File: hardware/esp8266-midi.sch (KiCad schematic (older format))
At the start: 26 parts, among them J1 MIDI in, J2 MIDI out, J3 TTL-232R-3V3 connector, J4 Bat+, J5 Bat-, J6 MIDI through, J7 Debug serial out, U1 ESP-12E, U2 6N138, U3 LD1117S50TR_SOT223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

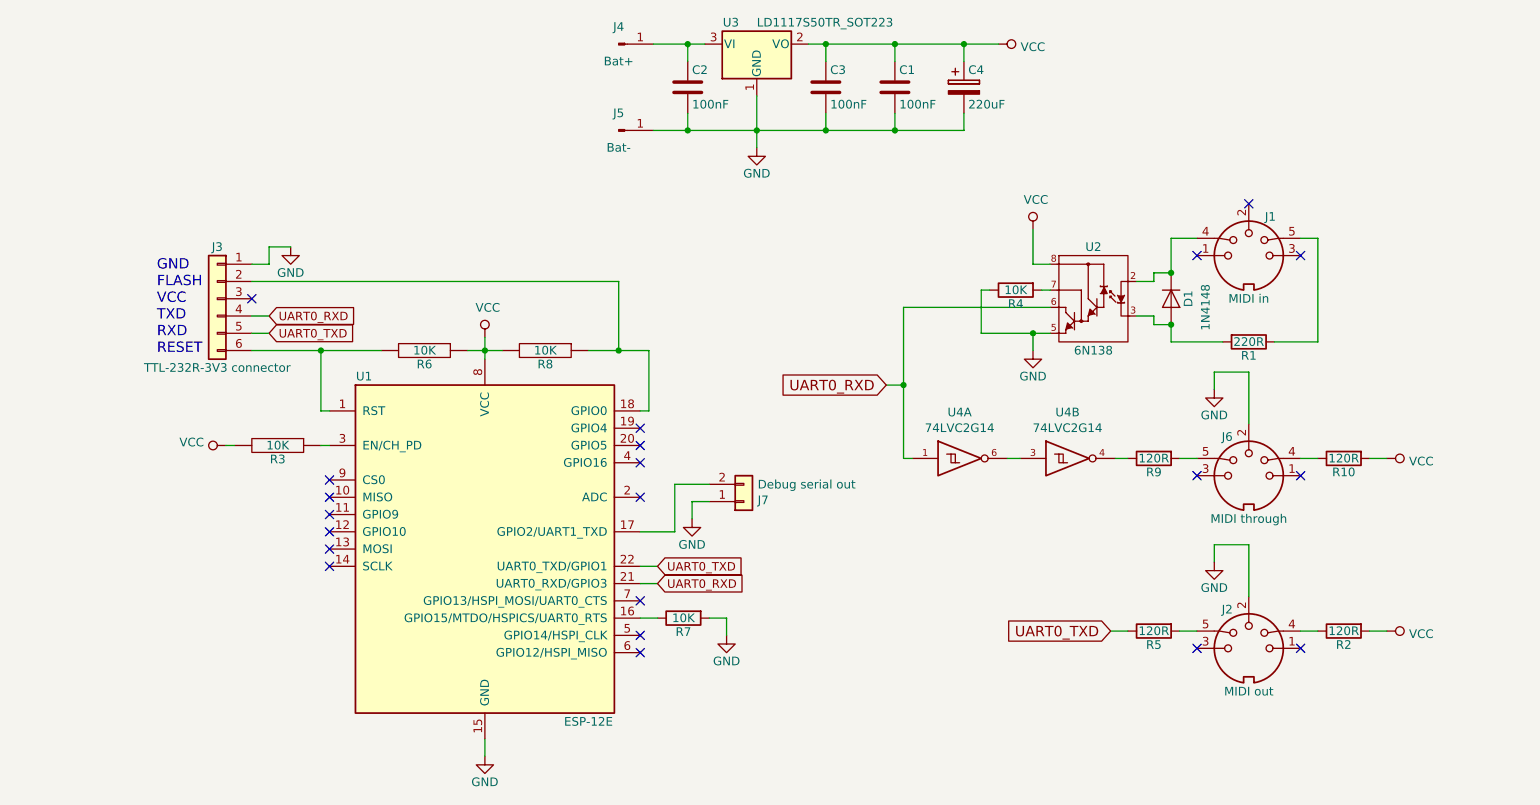
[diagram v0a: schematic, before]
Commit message: Misc: add some extra labels to have little more meaningful net names
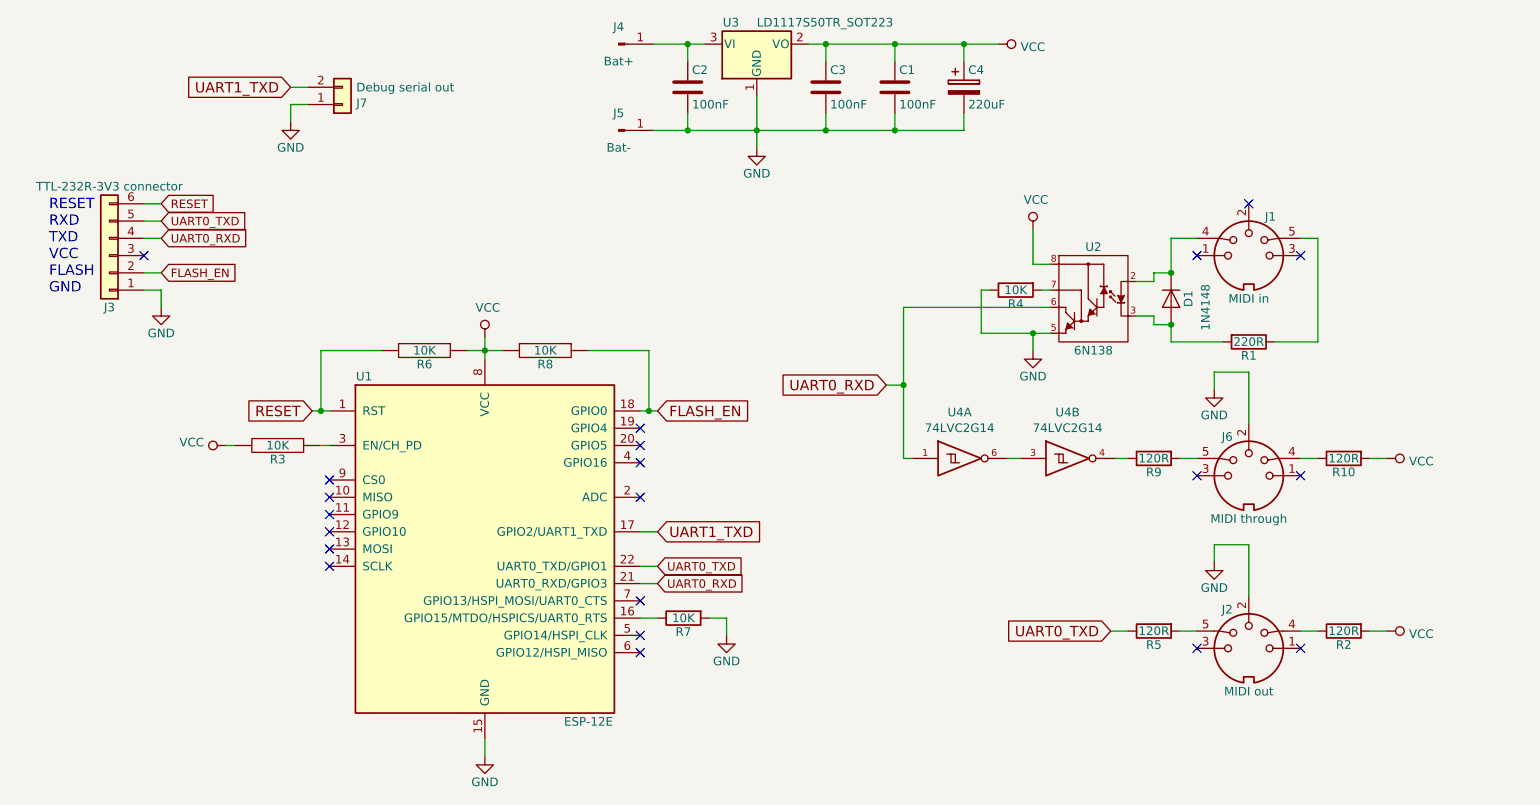
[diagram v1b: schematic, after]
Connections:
- net FLASH_EN: now reaches J3.2 (Pin_2), R8.1, U1.18 (GPIO0)
- net RESET: now reaches J3.6 (Pin_6), R6.2, U1.1 (RST)
- net UART1_TXD: now reaches J7.2 (Pin_2), U1.17 (GPIO2/UART1_TXD)
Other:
- note added: "RESET\nRXD\nTXD\nVCC\nFLASH\nGND\n"
- note removed: "GND\nFLASH\nVCC\nTXD\nRXD\nRESET"
- moved on the sheet: J3, J7
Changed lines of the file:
@@
 	-1   0    0    -1
 $EndComp
-Text Notes 2300 3475 0    60   ~ 0
-GND\nFLASH\nVCC\nTXD\nRXD\nRESET
+Text Notes 1675 3125 0    60   ~ 0
+RESET\nRXD\nTXD\nVCC\nFLASH\nGND\n
 NoConn ~ 8325 5175
 NoConn ~ 8925 5175
@@
 	4100 3450 4200 3450
 Wire Wire Line
-	4800 3450 4975 3450
-Wire Wire Line
 	5150 3450 5150 3800
 Wire Wire Line
@@
 L Connector1:Conn_01x06 J3
 U 1 1 5AA1FA8A
-P 2650 3150
-F 0 "J3" H 2650 3450 50  0000 C CNN
-F 1 "TTL-232R-3V3 connector" H 2650 2750 50  0000 C CNN
-F 2 "Pin_Headers:Pin_Header_Straight_1x06_Pitch2.54mm" H 2650 3150 50  0001 C CNN
-F 3 "" H 2650 3150 50  0001 C CNN
-	1    2650 3150
-	-1   0    0    -1
-$EndComp
-NoConn ~ 2850 3150
+P 2025 2900
+F 0 "J3" H 2025 3200 50  0000 C CNN
+F 1 "TTL-232R-3V3 connector" H 2025 2500 50  0000 C CNN
+F 2 "Pin_Headers:Pin_Header_Straight_1x06_Pitch2.54mm" H 2025 2900 50  0001 C CNN
+F 3 "" H 2025 2900 50  0001 C CNN
+	1    2025 2900
+	-1   0    0    1
+$EndComp
+NoConn ~ 2225 2900
 NoConn ~ 5100 4100
 Wire Wire Line
@@
 Wire Wire Line
 	6625 3200 7475 3200
-Text GLabel 2950 3350 2    49   Input ~ 0
+Text GLabel 2325 2700 2    49   Input ~ 0
 UART0_TXD
-Text GLabel 2950 3250 2    49   Input ~ 0
+Text GLabel 2325 2800 2    49   Input ~ 0
 UART0_RXD
 Wire Wire Line
@@
 Wire Wire Line
 	3250 3450 3600 3450
-Wire Wire Line
-	2850 3450 3250 3450
-Connection ~ 3250 3450
-Wire Wire Line
-	4975 3050 4975 3450
-Connection ~ 4975 3450
-Wire Wire Line
-	4975 3450 5150 3450
-Wire Wire Line
-	2850 3050 4975 3050
 $Comp
 L power1:GND #PWR05
 U 1 1 5C00E9E6
-P 3075 2850
-F 0 "#PWR05" H 3075 2600 50  0001 C CNN
-F 1 "GND" H 3075 2700 50  0000 C CNN
-F 2 "" H 3075 2850 50  0001 C CNN
-F 3 "" H 3075 2850 50  0001 C CNN
-	1    3075 2850
+P 2325 3200
+F 0 "#PWR05" H 2325 2950 50  0001 C CNN
+F 1 "GND" H 2325 3050 50  0000 C CNN
+F 2 "" H 2325 3200 50  0001 C CNN
+F 3 "" H 2325 3200 50  0001 C CNN
+	1    2325 3200
 	-1   0    0    -1
 $EndComp
-Wire Wire Line
-	2850 2950 2950 2950
-Wire Wire Line
-	2950 2950 2950 2850
-Wire Wire Line
-	2950 2850 3075 2850
-Wire Wire Line
-	2850 3250 2950 3250
-Wire Wire Line
-	2850 3350 2950 3350
 Text GLabel 5200 4700 2    49   Input ~ 0
 UART0_TXD
@@
 L Connector1:Conn_01x02 J7
 U 1 1 5C040B63
-P 5700 4325
-F 0 "J7" H 5780 4317 50  0000 L CNN
-F 1 "Debug serial out" H 5780 4226 50  0000 L CNN
-F 2 "Pin_Headers:Pin_Header_Straight_1x02_Pitch2.54mm" H 5700 4325 50  0001 C CNN
-F 3 "~" H 5700 4325 50  0001 C CNN
-	1    5700 4325
+P 3375 2025
+F 0 "J7" H 3455 2017 50  0000 L CNN
+F 1 "Debug serial out" H 3455 1926 50  0000 L CNN
+F 2 "Pin_Headers:Pin_Header_Straight_1x02_Pitch2.54mm" H 3375 2025 50  0001 C CNN
+F 3 "~" H 3375 2025 50  0001 C CNN
+	1    3375 2025
 	1    0    0    1
 $EndComp
-Wire Wire Line
-	5300 4500 5300 4225
 $Comp
 L power1:GND #PWR014
 U 1 1 5C0439C0
-P 5400 4425
-F 0 "#PWR014" H 5400 4175 50  0001 C CNN
-F 1 "GND" H 5400 4275 50  0000 C CNN
-F 2 "" H 5400 4425 50  0001 C CNN
-F 3 "" H 5400 4425 50  0001 C CNN
-	1    5400 4425
+P 3075 2125
+F 0 "#PWR014" H 3075 1875 50  0001 C CNN
+F 1 "GND" H 3075 1975 50  0000 C CNN
+F 2 "" H 3075 2125 50  0001 C CNN
+F 3 "" H 3075 2125 50  0001 C CNN
+	1    3075 2125
 	-1   0    0    -1
 $EndComp
 Wire Wire Line
-	5400 4425 5400 4325
-Wire Wire Line
-	5100 4500 5300 4500
+	3075 2125 3075 2025
 $Comp
 L esp8266-midi-rescue:C-RESCUE-esp8266-midi C1
@@
 	6975 1675 7175 1675
 $Comp
-L power:VCC #PWR?
+L power:VCC #PWR0101
 U 1 1 5C039076
 P 7175 1675
-F 0 "#PWR?" H 7175 1525 50  0001 C CNN
+F 0 "#PWR0101" H 7175 1525 50  0001 C CNN
 F 1 "VCC" V 7192 1803 50  0000 L CNN
 F 2 "" H 7175 1675 50  0001 C CNN
@@
 $EndComp
 $Comp
-L power:VCC #PWR?
+L power:VCC #PWR0102
 U 1 1 5C03C08A
 P 4200 3375
-F 0 "#PWR?" H 4200 3225 50  0001 C CNN
+F 0 "#PWR0102" H 4200 3225 50  0001 C CNN
 F 1 "VCC" H 4217 3548 50  0000 C CNN
 F 2 "" H 4200 3375 50  0001 C CNN
@@
 $EndComp
 $Comp
-L power:VCC #PWR?
+L power:VCC #PWR0103
 U 1 1 5C04A4B7
 P 2700 4000
-F 0 "#PWR?" H 2700 3850 50  0001 C CNN
+F 0 "#PWR0103" H 2700 3850 50  0001 C CNN
 F 1 "VCC" V 2718 4127 50  0000 L CNN
 F 2 "" H 2700 4000 50  0001 C CNN
@@
 $EndComp
 $Comp
-L power:VCC #PWR?
+L power:VCC #PWR0104
 U 1 1 5C0530C7
 P 7375 2750
-F 0 "#PWR?" H 7375 2600 50  0001 C CNN
+F 0 "#PWR0104" H 7375 2600 50  0001 C CNN
 F 1 "VCC" H 7392 2923 50  0000 C CNN
 F 2 "" H 7375 2750 50  0001 C CNN
@@
 $EndComp
 $Comp
-L power:VCC #PWR?
+L power:VCC #PWR0105
 U 1 1 5C05BBAA
 P 9425 4075
-F 0 "#PWR?" H 9425 3925 50  0001 C CNN
+F 0 "#PWR0105" H 9425 3925 50  0001 C CNN
 F 1 "VCC" V 9442 4203 50  0000 L CNN
 F 2 "" H 9425 4075 50  0001 C CNN
@@
 $EndComp
 $Comp
-L power:VCC #PWR?
+L power:VCC #PWR0106
 U 1 1 5C06708F
 P 9425 5075
-F 0 "#PWR?" H 9425 4925 50  0001 C CNN
+F 0 "#PWR0106" H 9425 4925 50  0001 C CNN
 F 1 "VCC" V 9442 5203 50  0000 L CNN
 F 2 "" H 9425 5075 50  0001 C CNN
@@
 $EndComp
 Wire Wire Line
-	5400 4325 5500 4325
-Wire Wire Line
-	5300 4225 5500 4225
+	3075 2025 3175 2025
+Text GLabel 5200 4500 2    60   Input ~ 0
+UART1_TXD
+Wire Wire Line
+	5100 4500 5200 4500
+Text GLabel 3075 1925 0    60   Input ~ 0
+UART1_TXD
+Wire Wire Line
+	3075 1925 3175 1925
+Text GLabel 5200 3800 2    60   Input ~ 0
+FLASH_EN
+Wire Wire Line
+	5150 3800 5200 3800
+Connection ~ 5150 3800
+Wire Wire Line
+	4800 3450 5150 3450
+Text GLabel 2325 3000 2    49   Input ~ 0
+FLASH_EN
+Text GLabel 3200 3800 0    60   Input ~ 0
+RESET
+Wire Wire Line
+	3200 3800 3250 3800
+Connection ~ 3250 3800
+Text GLabel 2325 2600 2    49   Input ~ 0
+RESET
+Wire Wire Line
+	2225 3100 2325 3100
+Wire Wire Line
+	2325 3100 2325 3200
+Wire Wire Line
+	2225 3000 2325 3000
+Wire Wire Line
+	2225 2600 2325 2600
+Wire Wire Line
+	2225 2800 2325 2800
+Wire Wire Line
+	2225 2700 2325 2700
 $EndSCHEMATC

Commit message: Use alternative uart0 pins for midi i/o
uart0 pushes bunch of rubbish messages on boot up. This means some pretty random
messages on the midi out port. To fix this midi i/o uses alternative uart0 pins
which can be enabled after microcontroller is booted by calling 'Serial.swap()'.

Alternative TX pin needs to be pulled down during boot, but a connected midi
instrument pull it up. Therefore the buffering using the same dual nand
(74LVC2G14) as for the midi through port.
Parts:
- added C5: 100nF, Capacitors_SMD:C_0805_HandSoldering, symbol esp8266-midi-rescue:C-RESCUE-esp8266-midi
- added U5: 74LVC2G14, TO_SOT_Packages_SMD:SOT-23-6_Handsoldering, symbol 74xGxx:74LVC2G14
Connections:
- net GND: now also R7.1, C5.2, U5.2 (GND), U5.2 (GND); no longer R7.2
- net UART0_RXD: no longer U2.6 (Vo), U4.1
- net UART0_TXD: no longer R5.1
- net VCC: now also C5.1, U5.5 (VCC), U5.5 (VCC)
- net UART0_ALT_TXD: now reaches U1.16 (GPIO15/MTDO/HSPICS/UART0_RTS)
- net UART0_ALT_TXD: now also R7.2, U5.1; no longer R7.1
- net UART0_ALT_RXD: now reaches U1.7 (GPIO13/HSPI_MOSI/UART0_CTS)
- net UART0_ALT_RXD: now also U2.6 (Vo), U4.1
- new net: R5.1, U5.4
- new net: U5.3, U5.6
- no-connect marks 21 -> 20
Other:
- moved on the sheet: C4, D1, J1, J2, J6, R1, R10, R2, R4, R5, R7, R9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

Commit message: Kicad5 update woes again: eeschema rescues
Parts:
- C4: symbol device:CP -> esp8266-midi-rescue:CP-device
- D1: symbol device:D -> esp8266-midi-rescue:D-device
- J1, J2, J6: symbol Connector1:DIN-5_180degree -> esp8266-midi-rescue:DIN-5_180degree-Connector1
- J3: symbol Connector1:Conn_01x06 -> esp8266-midi-rescue:Conn_01x06-Connector1
- J4, J5: symbol Connector1:Conn_01x01_Male -> esp8266-midi-rescue:Conn_01x01_Male-Connector1
- J7: symbol Connector1:Conn_01x02 -> esp8266-midi-rescue:Conn_01x02-Connector1
- R3, R6, R8: symbol pspice1:R -> esp8266-midi-rescue:R-pspice1
- U1: symbol rfcom:ESP-12E -> esp8266-midi-rescue:ESP-12E-rfcom
- U3: symbol regul:LD1117S50TR_SOT223 -> esp8266-midi-rescue:LD1117S50TR_SOT223-regul
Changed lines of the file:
@@
 $EndDescr
 $Comp
-L Connector1:DIN-5_180degree J2
+L esp8266-midi-rescue:DIN-5_180degree-Connector1 J2
 U 1 1 5AA0E52B
 P 9125 5175
@@
 $EndComp
 $Comp
-L Connector1:DIN-5_180degree J1
+L esp8266-midi-rescue:DIN-5_180degree-Connector1 J1
 U 1 1 5AA0E5AD
 P 9125 2900
@@
 $EndComp
 $Comp
-L power1:GND #PWR01
+L esp8266-midi-rescue:GND-power1 #PWR01
 U 1 1 5AA0E6C2
 P 8925 4675
@@
 $EndComp
 $Comp
-L device:D D1
+L esp8266-midi-rescue:D-device D1
 U 1 1 5AA1AFB6
 P 8675 3150
@@
 $EndComp
 $Comp
-L power1:GND #PWR04
+L esp8266-midi-rescue:GND-power1 #PWR04
 U 1 1 5AA1CB1B
 P 7875 3450
@@
 NoConn ~ 9425 2900
 $Comp
-L regul:LD1117S50TR_SOT223 U3
+L esp8266-midi-rescue:LD1117S50TR_SOT223-regul U3
 U 1 1 5AA2FC6F
 P 5775 1675
@@
 $EndComp
 $Comp
-L device:CP C4
+L esp8266-midi-rescue:CP-device C4
 U 1 1 5AA30545
 P 7375 1925
@@
 $EndComp
 $Comp
-L power1:GND #PWR07
+L esp8266-midi-rescue:GND-power1 #PWR07
 U 1 1 5AA310B5
 P 5775 2275
@@
 $EndComp
 $Comp
-L Connector1:Conn_01x01_Male J4
+L esp8266-midi-rescue:Conn_01x01_Male-Connector1 J4
 U 1 1 5AA3271F
 P 4975 1675
@@
 $EndComp
 $Comp
-L Connector1:Conn_01x01_Male J5
+L esp8266-midi-rescue:Conn_01x01_Male-Connector1 J5
 U 1 1 5AA327AB
 P 4975 2175
@@
 NoConn ~ 9125 2600
 $Comp
-L rfcom:ESP-12E U1
+L esp8266-midi-rescue:ESP-12E-rfcom U1
 U 1 1 5AC3DEE1
 P 4200 4600
@@
 $EndComp
 $Comp
-L power1:GND #PWR08
+L esp8266-midi-rescue:GND-power1 #PWR08
 U 1 1 5AC3E798
 P 4200 5800
@@
 $EndComp
 $Comp
-L power1:GND #PWR011
+L esp8266-midi-rescue:GND-power1 #PWR011
 U 1 1 5AC41342
 P 5250 5500
@@
 NoConn ~ 5100 4300
 $Comp
-L pspice1:R R6
+L esp8266-midi-rescue:R-pspice1 R6
 U 1 1 5B127227
 P 3850 3450
@@
 $EndComp
 $Comp
-L pspice1:R R8
+L esp8266-midi-rescue:R-pspice1 R8
 U 1 1 5B1275B7
 P 4550 3450
@@
 	3250 3800 3300 3800
 $Comp
-L pspice1:R R3
+L esp8266-midi-rescue:R-pspice1 R3
 U 1 1 5B12802D
 P 3000 4000
@@
 	2750 4000 2700 4000
 $Comp
-L Connector1:Conn_01x06 J3
+L esp8266-midi-rescue:Conn_01x06-Connector1 J3
 U 1 1 5AA1FA8A
 P 2025 2900
@@
 $EndComp
 $Comp
-L Connector1:DIN-5_180degree J6
+L esp8266-midi-rescue:DIN-5_180degree-Connector1 J6
 U 1 1 5BF9BC6A
 P 9125 4175
@@
 $EndComp
 $Comp
-L power1:GND #PWR012
+L esp8266-midi-rescue:GND-power1 #PWR012
 U 1 1 5BF9BC71
 P 8925 3675
@@
 	3250 3450 3600 3450
 $Comp
-L power1:GND #PWR05
+L esp8266-midi-rescue:GND-power1 #PWR05
 U 1 1 5C00E9E6
 P 2325 3200
@@
 NoConn ~ 5100 4000
 $Comp
-L Connector1:Conn_01x02 J7
+L esp8266-midi-rescue:Conn_01x02-Connector1 J7
 U 1 1 5C040B63
 P 3375 2025
@@
 $EndComp
 $Comp
-L power1:GND #PWR014
+L esp8266-midi-rescue:GND-power1 #PWR014
 U 1 1 5C0439C0
 P 3075 2125
